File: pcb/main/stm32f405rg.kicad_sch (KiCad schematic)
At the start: 49 parts, among them J11 Conn_ARM_JTAG_SWD_10, J12 UART1 SH, J13 Micro_SD_Card, J14 PH 2.0, Q1 BSS138, SW1 RESET, SW2 USER, U2 STM32F405RGTx, U3 MCP2562-E-SN, Y1 XRCGB16M000FXN02R0

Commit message: feat: finish main board v2
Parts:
- removed R9: 120, Resistor_SMD:R_0603_1608Metric_Pad0.98x0.95mm_HandSolder, symbol Device:R_Small
- added H1, H2, H3, H4: MountingHole, MountingHole:MountingHole_3.2mm_M3_Pad_TopBottom, symbol Mechanical:MountingHole
- added H5, H6, H7, H8: MountingHole, MountingHole:MountingHole_2.2mm_M2_ISO14580_Pad, symbol Mechanical:MountingHole
- added R16, R17: 120, Resistor_SMD:R_0603_1608Metric_Pad0.98x0.95mm_HandSolder, symbol Device:R_Small
- D3: renamed from D2; footprint LED_SMD:LED_0402_1005Metric -> LED_SMD:LED_0603_1608Metric
- D4: renamed from D3; footprint LED_SMD:LED_0402_1005Metric -> LED_SMD:LED_0603_1608Metric
- D5: renamed from D4; footprint LED_SMD:LED_0402_1005Metric -> LED_SMD:LED_0603_1608Metric
- D6: renamed from D5; footprint LED_SMD:LED_0402_1005Metric -> LED_SMD:LED_0603_1608Metric
- D7: renamed from D6; footprint LED_SMD:LED_0402_1005Metric -> LED_SMD:LED_0603_1608Metric
- D8: renamed from D7; footprint LED_SMD:LED_0402_1005Metric -> LED_SMD:LED_0603_1608Metric
- J13: renamed from J11; footprint Connector_PinHeader_1.27mm:PinHeader_2x05_P1.27mm_Vertical -> mylib:322110010000
- J14: renamed from J12; footprint Connector_PinHeader_2.54mm:PinHeader_1x04_P2.54mm_Horizontal -> Connector_PinHeader_2.54mm:PinHeader_1x04_P2.54mm_Vertical
- renumbered C11 to C10, C12 to C11, C13 to C12, C14 to C13, C15 to C14, C5 to C15, C8 to C16, C16 to C17, C9 to C8, C10 to C9, J13 to J11, J14 to J12, R4 to R10, R5 to R11, R6 to R12, R7 to R13, R3 to R14, R8 to R15, R10 to R18, R11 to R19, R12 to R20, R13 to R21, R14 to R22, R15 to R23, R16 to R24, R2 to R4, R17 to R5, R18 to R6, R19 to R7, R20 to R8, R21 to R9, U2 to U3, U3 to U4
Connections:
- net +3.3V: now also J12.1 (Pin_1)
- net +5V: no longer J12.1 (Pin_1)
- net CAN_H: now also R16.1
- net CAN_L: now also R16.2
- net LCD_RST: now also U3.16 (PA2); no longer U3.15 (PA1)
- net LED_CAN_RX: now also U3.33 (PB12); no longer U3.38 (PC7)
- net LED_CAN_TX: now also U3.36 (PB15); no longer U3.41 (PA8)
- net SPI1_CS: now also U3.15 (PA1); no longer U3.14 (PA0)
- net SW1: now also U3.14 (PA0); no longer U3.16 (PA2)
- net TIM12_SP: now also R17.1; no longer Q1.1 (G), R18.1
- net ADC1_IN9 renamed ADC_BATTERY
- net SPI2_SCK renamed SPI2_CLK
- net SPI3_MISO renamed SPI2_MISO
- net SPI3_MOSI renamed SPI2_MOSI
- new net: Q1.1 (G), R17.2, R18.1
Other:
- moved on the sheet: Q1, R18, SP1

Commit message: perf: edit SW footprint
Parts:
- SW1, SW2: footprint bldc_lib:SKRPACE010 -> mylib:TVAF06A020BR
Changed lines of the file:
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@@
 			)
 		)
-		(property "Footprint" "bldc_lib:SKRPACE010"
+		(property "Footprint" "mylib:TVAF06A020BR"
 			(at 219.71 115.57 0)
 			(effects
@@
 			)
 		)
-		(property "Footprint" "bldc_lib:SKRPACE010"
+		(property "Footprint" "mylib:TVAF06A020BR"
 			(at 170.18 114.3 0)
 			(effects

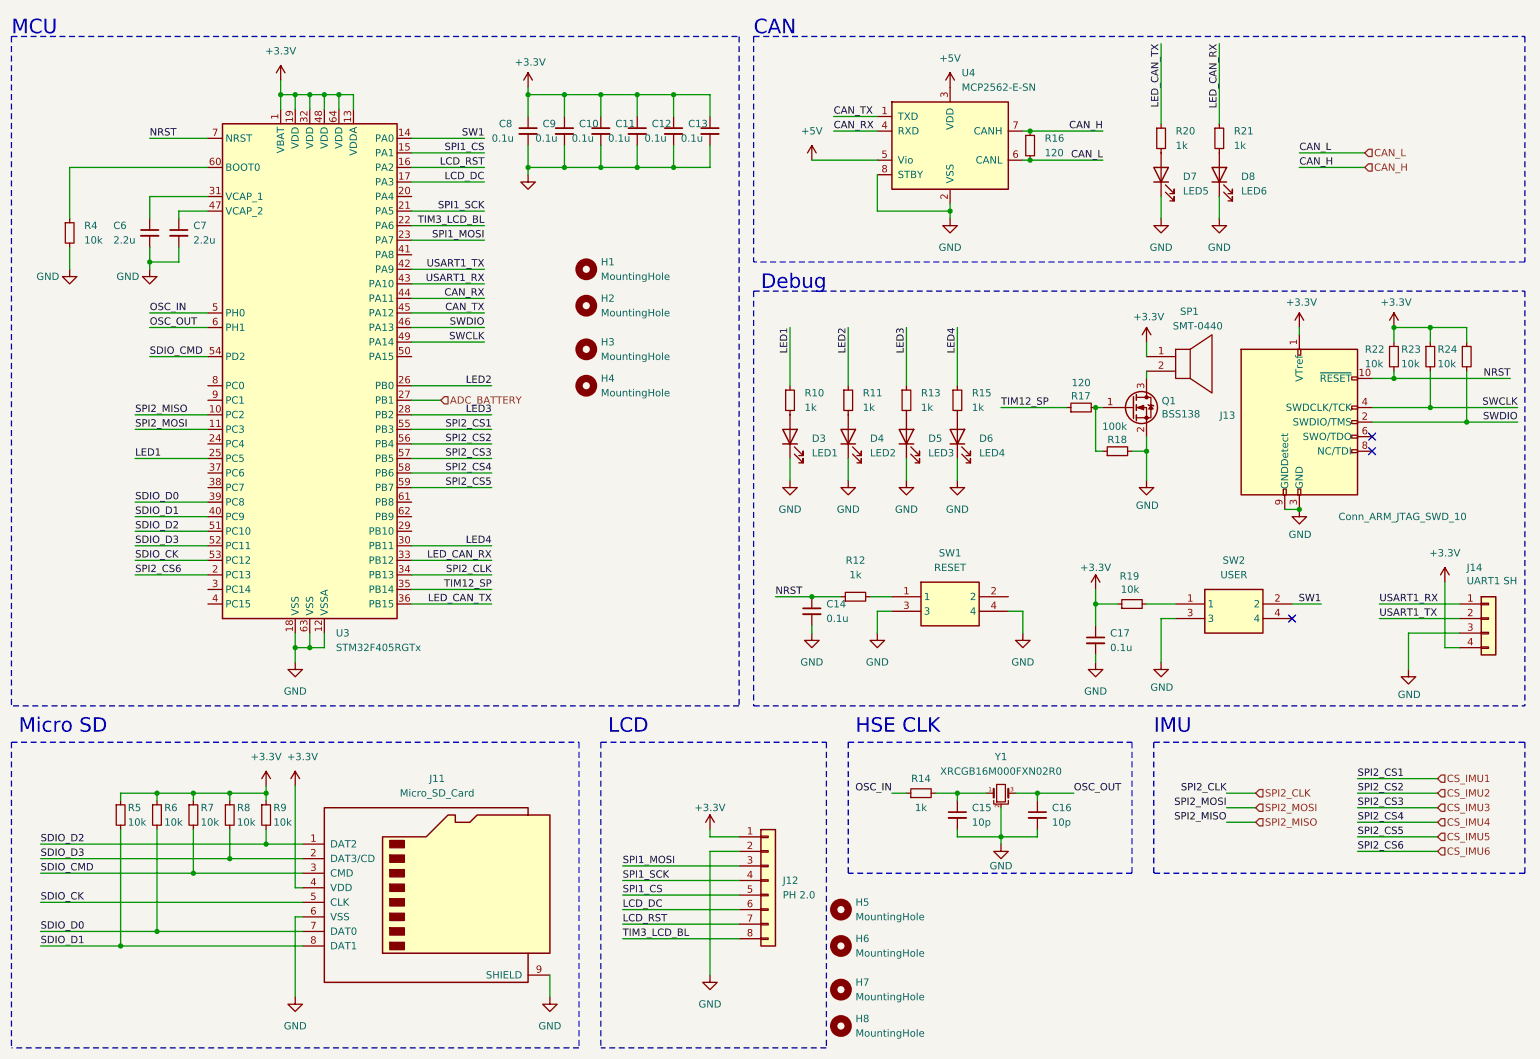
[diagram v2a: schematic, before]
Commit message: feat: delete two CAN connectors & add microSD input pin
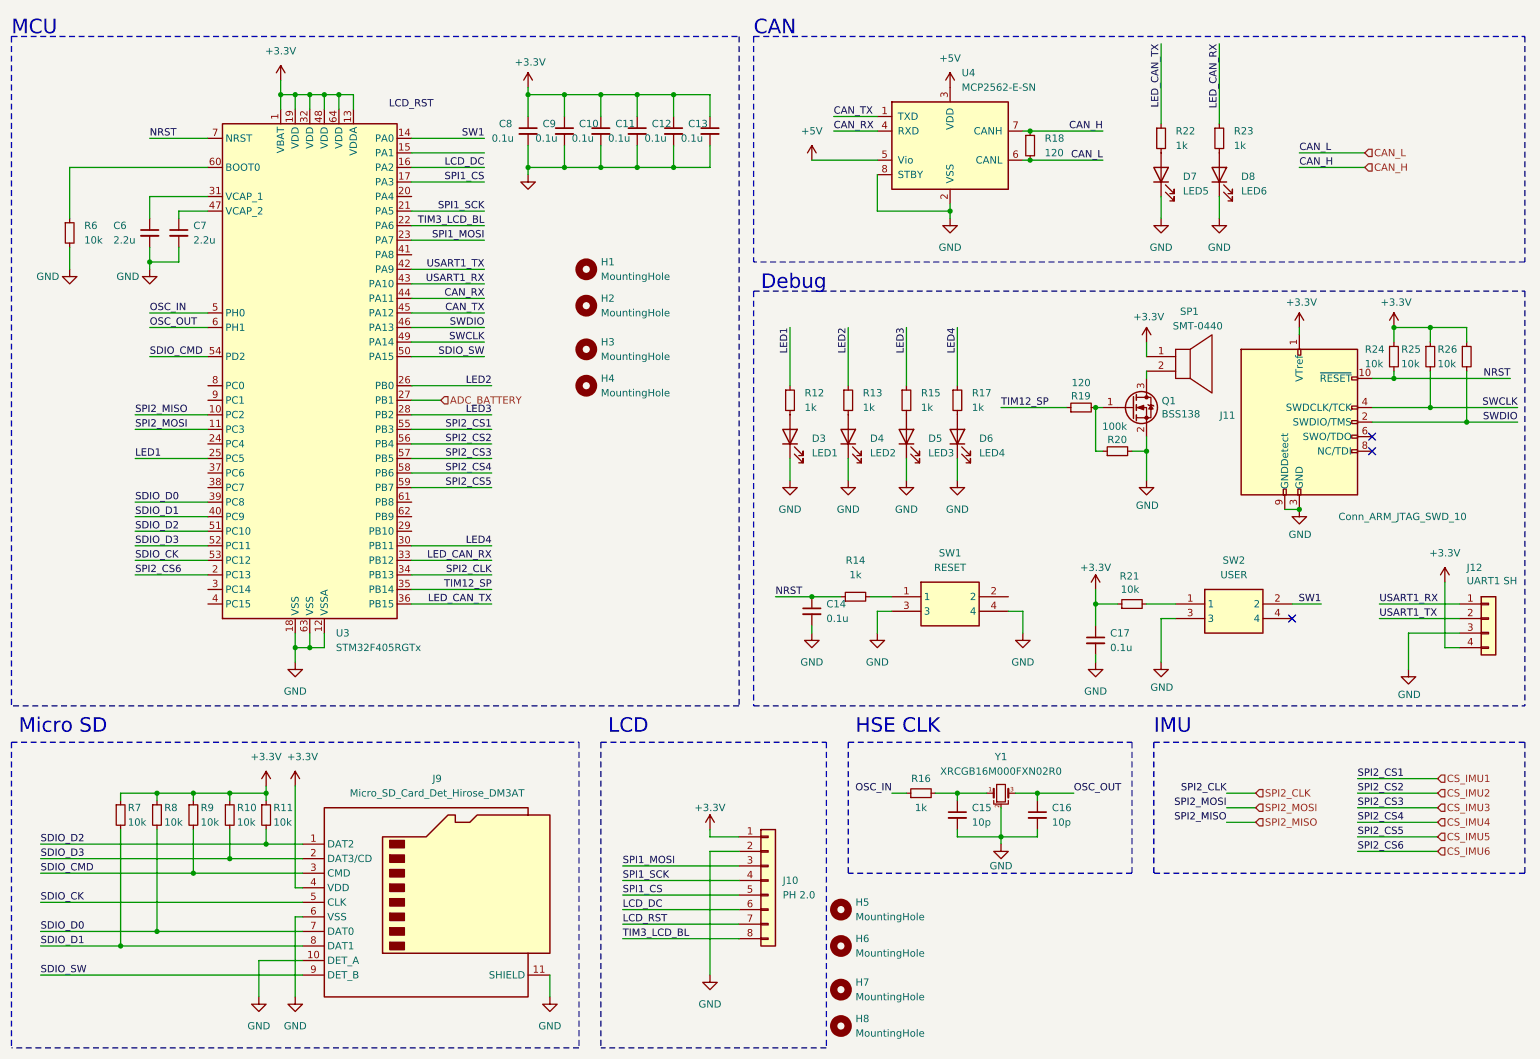
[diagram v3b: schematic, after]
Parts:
- removed J11: Micro_SD_Card, Connector_Card:microSD_HC_Hirose_DM3AT-SF-PEJM5, symbol Connector:Micro_SD_Card
- added J9: Micro_SD_Card_Det_Hirose_DM3AT, Connector_Card:microSD_HC_Hirose_DM3AT-SF-PEJM5, symbol Connector:Micro_SD_Card_Det_Hirose_DM3AT
- renumbered J12 to J10, J13 to J11, J14 to J12, R8 to R10, R9 to R11, R10 to R12, R11 to R13, R12 to R14, R13 to R15, R14 to R16, R15 to R17, R16 to R18, R17 to R19, R18 to R20, R19 to R21, R20 to R22, R21 to R23, R22 to R24, R23 to R25, R24 to R26, R4 to R6, R5 to R7, R6 to R8, R7 to R9
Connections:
- net +3.3V: now also J9.4 (VDD)
- net GND: now also J9.10 (DET_A), J9.11 (SHIELD), J9.6 (VSS)
- net LCD_DC: now also U3.16 (PA2); no longer U3.17 (PA3)
- net LCD_RST: no longer U3.16 (PA2)
- net SDIO_CK: now also J9.5 (CLK)
- net SDIO_CMD: now also J9.3 (CMD)
- net SDIO_D0: now also J9.7 (DAT0)
- net SDIO_D1: now also J9.8 (DAT1)
- net SDIO_D2: now also J9.1 (DAT2)
- net SDIO_D3: now also J9.2 (DAT3/CD)
- net SPI1_CS: now also U3.17 (PA3); no longer U3.15 (PA1)
- net SDIO_SW: now reaches U3.50 (PA15)
- net SDIO_SW: now also J9.9 (DET_B)
